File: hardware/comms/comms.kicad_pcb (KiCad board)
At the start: 4 copper layers, 28 x 63 mm, 78 parts, among them J1 USB-C, J2 LEFT, J3 RIGHT, J4 SWD, Q1 MMBT3904, SW1 BOOTSEL, SW2 RUN, U1 RP2350A, U10 TS3USB221A, U2 AMS1117-3.3, U3 W25Q16JVUXIQ, U4 ST60A3H1, U5 PTN3222GM, U6 TXS0108E, U7 TLV75518P, U8 USBLC6-2SC6, U9 TS3USB221A, Y1 12MHz

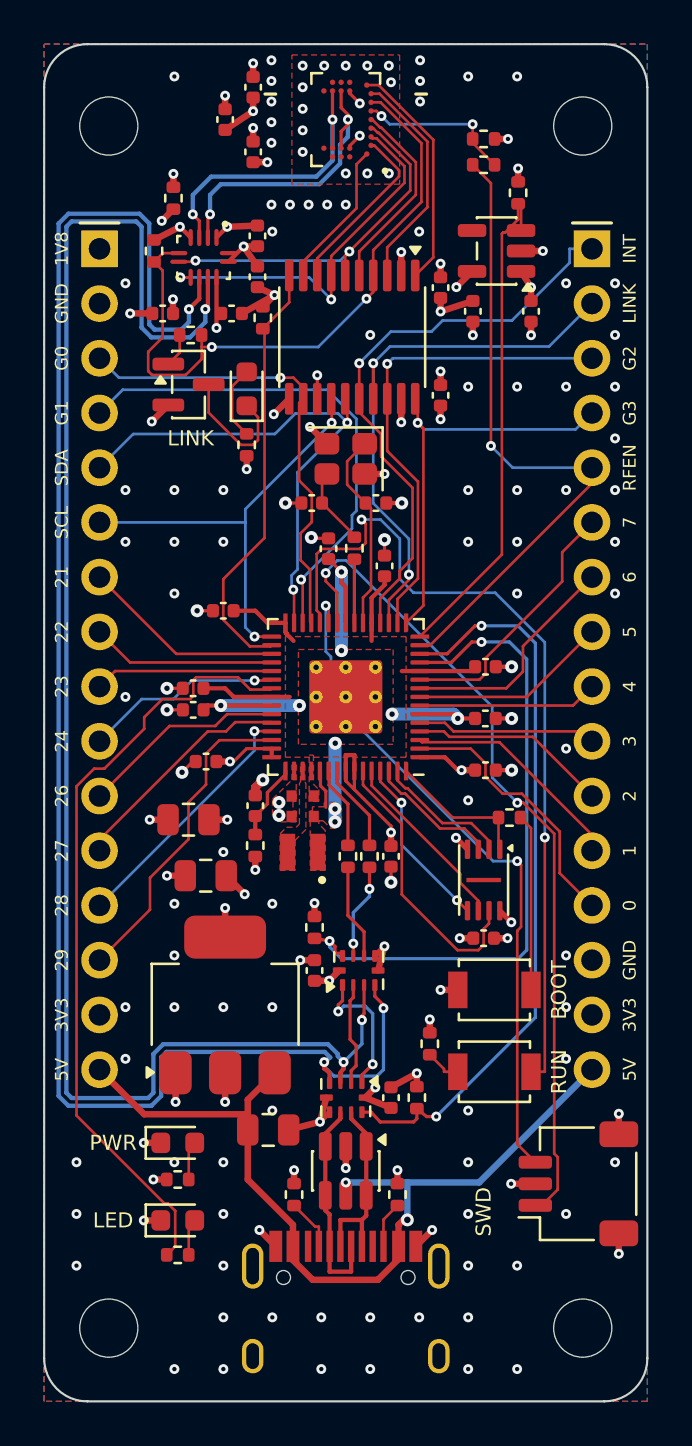
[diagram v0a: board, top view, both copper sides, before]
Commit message: Rev A after review: ST's antenna ground, 1.8 V rail, pull-ups, 90 ohm pairs
Two independent reviews (schematic against the data sheets, layout
against JLCPCB's limits and ST's B2379A) found no blocker and a dozen
things worth fixing. The board is regenerated and routed again.

Layout: the ST60's ball field is laid as ST lays it -- nine signals
straight out through one side of the ring, the supply along the top --
and the island and fence vias are ST's own, from its drill file (33 and
45 fit, where rev A had 13 and 15). USB pairs on the back 0.28/0.16 mm;
the +1V8 plane redrawn so the pair to the repeater has +3V3 under it
throughout. ST60 mask openings 0.30 mm. Silkscreen to JLCPCB's sizes.
VBUS joined on the back, not under the USB-C shell. Three fiducials.

Schematic: 1.8 uF on +1V8 and its enable pulled down; 4k7 on MODE_INT;
4k7 pull-ups on the 1.8 V side of the four I2C lines; 220 R on the LEDs.

README has the review table, what was left as it is, and ordering notes
(Standard PCBA, 0.10 mm stencil, nylon standoffs, firmware sequencing).

Co-Authored-By: Claude Fable 5.1 <noreply@anthropic.com>
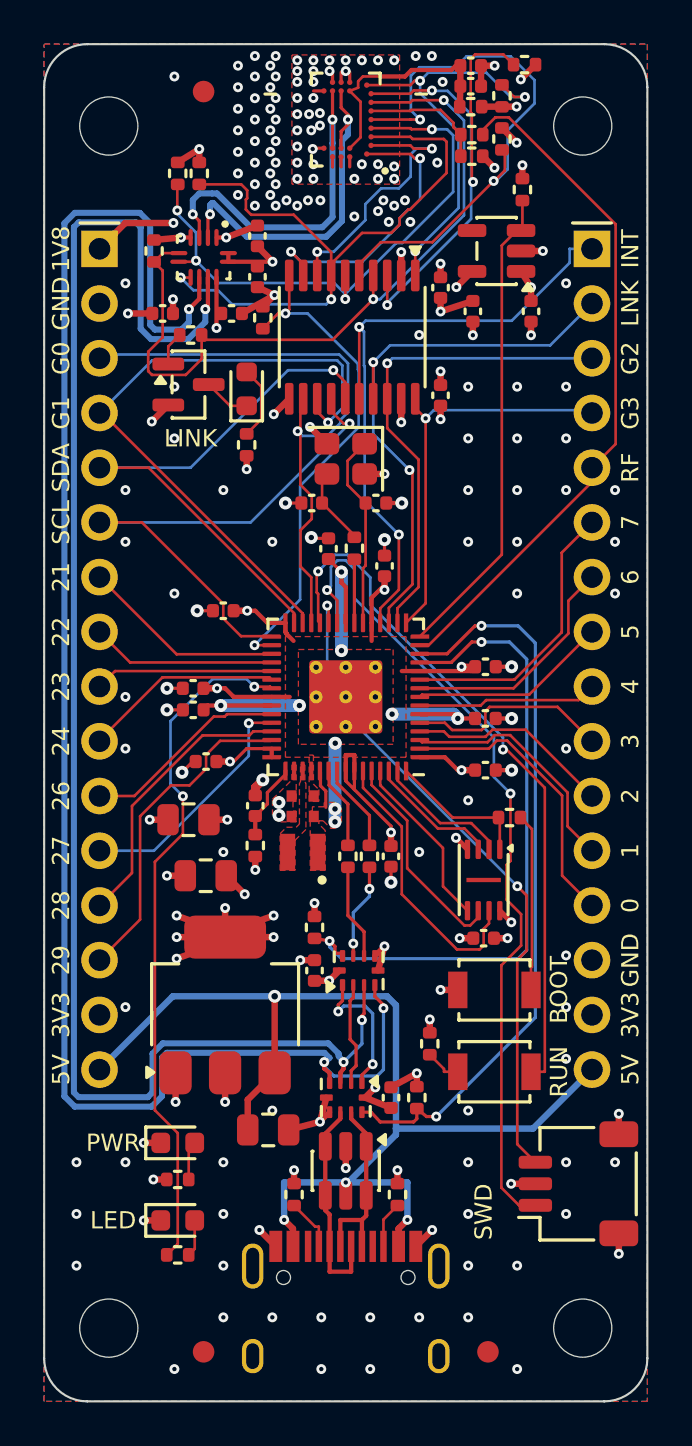
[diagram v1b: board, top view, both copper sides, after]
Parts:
- removed C23: 1u, Capacitor_SMD:C_0402_1005Metric
- added FID1: Fiducial, Fiducial:Fiducial_1mm_Mask2mm, F.Cu at (93.4, 42.2)
- added FID2: Fiducial, Fiducial:Fiducial_1mm_Mask2mm, F.Cu at (93.4, 100.7)
- added FID3: Fiducial, Fiducial:Fiducial_1mm_Mask2mm, F.Cu at (106.6, 100.7)
- added R24: 4k7, Resistor_SMD:R_0402_1005Metric, F.Cu at (93.2, 46.0)
- added R25: 4k7, Resistor_SMD:R_0402_1005Metric, F.Cu at (92.2, 46.0)
- added R26: 4k7, Resistor_SMD:R_0402_1005Metric, F.Cu at (108.3, 41.0)
- added R27: 4k7, Resistor_SMD:R_0402_1005Metric, F.Cu at (107.2, 42.4)
- added R31: 4k7, Resistor_SMD:R_0402_1005Metric, F.Cu at (107.2, 44.4)
- C26: value 1u -> 470n
- R14, R30, R9: value 1k -> 220R
- R15: value 10k -> 4k7
- moved R20 14.4 mm to (105.8, 42.9), turned to 180 degrees
- moved C21 10.6 mm to (105.8, 42.0), turned to 0 degrees
- moved C22 10.1 mm to (105.8, 41.0), turned to 0 degrees
- moved R21 1.50 mm to (105.8, 44.2), turned to 180 degrees
- moved R22 0.97 mm to (105.8, 45.2)
- moved R15 0.25 mm to (108.2, 46.8)
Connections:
- R15 pad 1: +3V3 -> GND
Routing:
- net ST_MODE_INT: track 9.24 -> 26.7 mm, vias 0 -> 2
- net ST_G2: track 10.5 -> 25.1 mm, vias 0 -> 3
- net ST_SCL: track 17.6 -> 30.7 mm
- net VBUS: track 41.5 -> 53.5 mm, vias 2 -> 4
- net ST_SDA: track 17.0 -> 27.2 mm, vias 2 -> 4
- net ST_G3: track 10.8 -> 20.0 mm, vias 0 -> 3
- net +1V8: track 7.87 -> 16.1 mm, vias 5 -> 8
- net RUN: track 39.4 -> 32.7 mm
- net TUN_G0: track 21.7 -> 28.2 mm
- net ST_G0: track 6.86 -> 13.4 mm, vias 0 -> 2
- net ST_VDD: track 5.02 -> 10.7 mm, vias 5 -> 0
- net CFG_SCL: track 20.4 -> 25.8 mm, vias 2 -> 1
- net TUN_G1: track 25.3 -> 30.3 mm, vias 2 -> 1
- net GND: track 52.1 -> 57.0 mm, vias 153 -> 194
- net ST_LINK_STATUS: track 30.8 -> 35.6 mm
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- removed copper zone on In2.Cu, net ST_VDD
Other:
- board text added: "60 GHz ANTENNA THIS END"
- board text added: "KEEP CLEAR"
- board text added: "LNK"
- board text added: "RF"
- board text removed: "60 GHz ANTENNA THIS END - KEEP CLEAR"

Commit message: Rev B: OV2640 camera connector on the back, six layers
A 24-way flex connector (FH12-24S-0.5SH) for the common OV2640 module,
on the back of the board so the lens looks away from the link partner,
with 2.8 V and 1.3 V regulators, pull-ups and decoupling. The camera's
signals are header GPIO (0-7 data, 21 VSYNC, 22/23 SCCB, 24 PWDN,
26 HREF, 27 XCLK, 28 PCLK), wired by hand on the back from the headers'
own pads to the connector, none crossing.

Six layers (JLC06161H-7628, same outer prepreg as the four-layer stack):
with the back layer taken the board would not route on four. Parts on
the back keep their vias out of the RP2350's fan-out gaps.

An independent check confirmed the connector's pin order and contact
side against two module drawings and Hirose's data sheet, and its
findings are in: 1.3 V core, 100 n at the connector, wider supply
tracks, more room round XCLK, the module outline moved.

DRC, ERC, netlist and assembly checks pass; viewer rebuilt.

Co-Authored-By: Claude Fable 5.1 <noreply@anthropic.com>
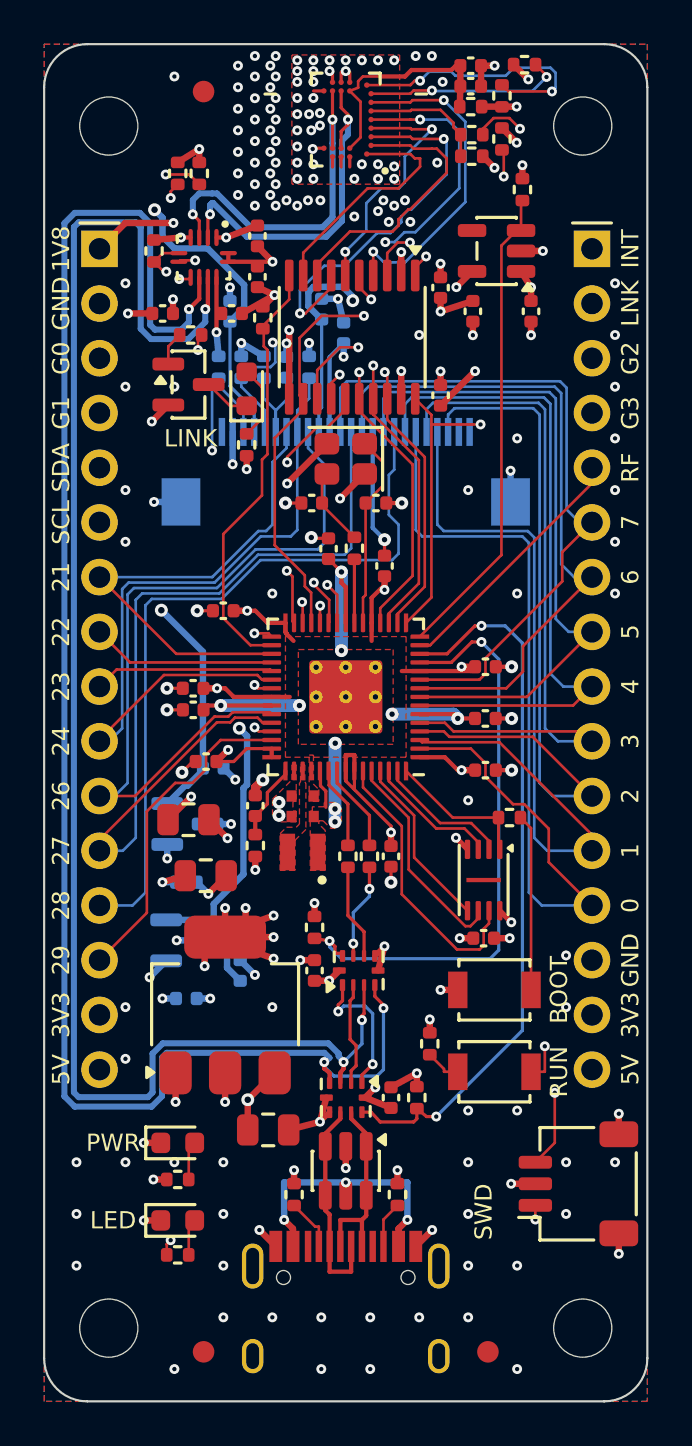
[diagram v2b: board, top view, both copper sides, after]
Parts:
- added C40: 1u, Capacitor_SMD:C_0402_1005Metric, B.Cu at (92.6, 78.9)
- added C41: 1u, Capacitor_SMD:C_0402_1005Metric, B.Cu at (93.8, 73.6)
- added C42: 1u, Capacitor_SMD:C_0402_1005Metric, B.Cu at (95.1, 83.0)
- added C43: 1u, Capacitor_SMD:C_0402_1005Metric, B.Cu at (97.2, 55.0)
- added C44: 1u, Capacitor_SMD:C_0402_1005Metric, B.Cu at (92.6, 84.3)
- added C45: 100n, Capacitor_SMD:C_0402_1005Metric, B.Cu at (94.6, 52.4)
- added C46: 100n, Capacitor_SMD:C_0402_1005Metric, B.Cu at (98.9, 52.3)
- added C47: 100n, Capacitor_SMD:C_0402_1005Metric, B.Cu at (99.9, 53.4)
- added J5: OV2640, Connector_FFC-FPC:Hirose_FH12-24S-0.5SH_1x24-1MP_P0.50mm_Horizontal, B.Cu at (100.0, 59.9)
- added R40: 4k7, Resistor_SMD:R_0402_1005Metric, B.Cu at (94.1, 55.0)
- added R41: 4k7, Resistor_SMD:R_0402_1005Metric, B.Cu at (95.2, 55.0)
- added R42: 10k, Resistor_SMD:R_0402_1005Metric, B.Cu at (96.2, 55.0)
- added R43: 10k, Resistor_SMD:R_0402_1005Metric, B.Cu at (98.3, 55.0)
- added U11: XC6206P282MR, Package_TO_SOT_SMD:SOT-23, B.Cu at (92.7, 76.2)
- added U12: ME6216A13M3G, Package_TO_SOT_SMD:SOT-23, B.Cu at (92.6, 81.6)
- turned R26 to 180 degrees
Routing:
- net CAM_1V3: track 0.00 -> 46.4 mm, vias 0 -> 2
- net CAM_2V8: track 0.00 -> 42.7 mm, vias 0 -> 2
- net GP28: track 13.2 -> 46.1 mm, vias 0 -> 1
- net GP27: track 11.3 -> 39.9 mm, vias 1 -> 0
- net GP0: track 13.5 -> 41.3 mm
- net GP26: track 9.57 -> 35.1 mm
- net GP23: track 8.29 -> 33.0 mm, vias 0 -> 1
- net GP1: track 11.3 -> 36.0 mm
- net GP2: track 9.51 -> 33.9 mm
- net GP24: track 9.29 -> 32.8 mm
- net GP4: track 8.36 -> 30.9 mm
- net GP3: track 9.65 -> 31.9 mm
- net GND: track 57.0 -> 78.8 mm
- net GP5: track 9.24 -> 30.8 mm
- net GP6: track 11.0 -> 31.3 mm
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- added copper zone on In4.Cu, net +1V8
- added copper zone on In4.Cu, net +3V3
- added copper zone on In2.Cu, net GND
- added copper zone on In3.Cu, net GND
- removed copper zone on In2.Cu, net +1V8
- removed copper zone on In2.Cu, net +3V3
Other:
- copper layers 4 -> 6
- board text added: "LENS UP"
- board text added: "OV2640"
- board text added: "RP2350A + ST60A3H1"
- board text added: "comms rev B"
- board text removed: "GP0"
- board text removed: "GP1"
- board text removed: "GP2"
- board text removed: "GP21"
- board text removed: "GP22"
- board text removed: "GP23"
- board text removed: "GP24"
- board text removed: "GP26"
- board text removed: "GP27"
- board text removed: "GP28"
- board text removed: "GP29"
- board text removed: "GP3"
- board text removed: "GP4"
- board text removed: "GP5"
- board text removed: "GP6"
- board text removed: "GP7"
- board text removed: "KEEP CLEAR"
- board text removed: "RFEN"
- board text removed: "comms rev A RP2350A + ST60A3H1"
